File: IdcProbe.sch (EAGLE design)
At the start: 78 parts, among them P1 BANANA_SOCKETVERTICAL, P2 BANANA_SOCKETVERTICAL, Q1 PMV45EN, U1 TPS65131RGET, U2 NCP361MUTBG, U4 TL074D, X3 R141426

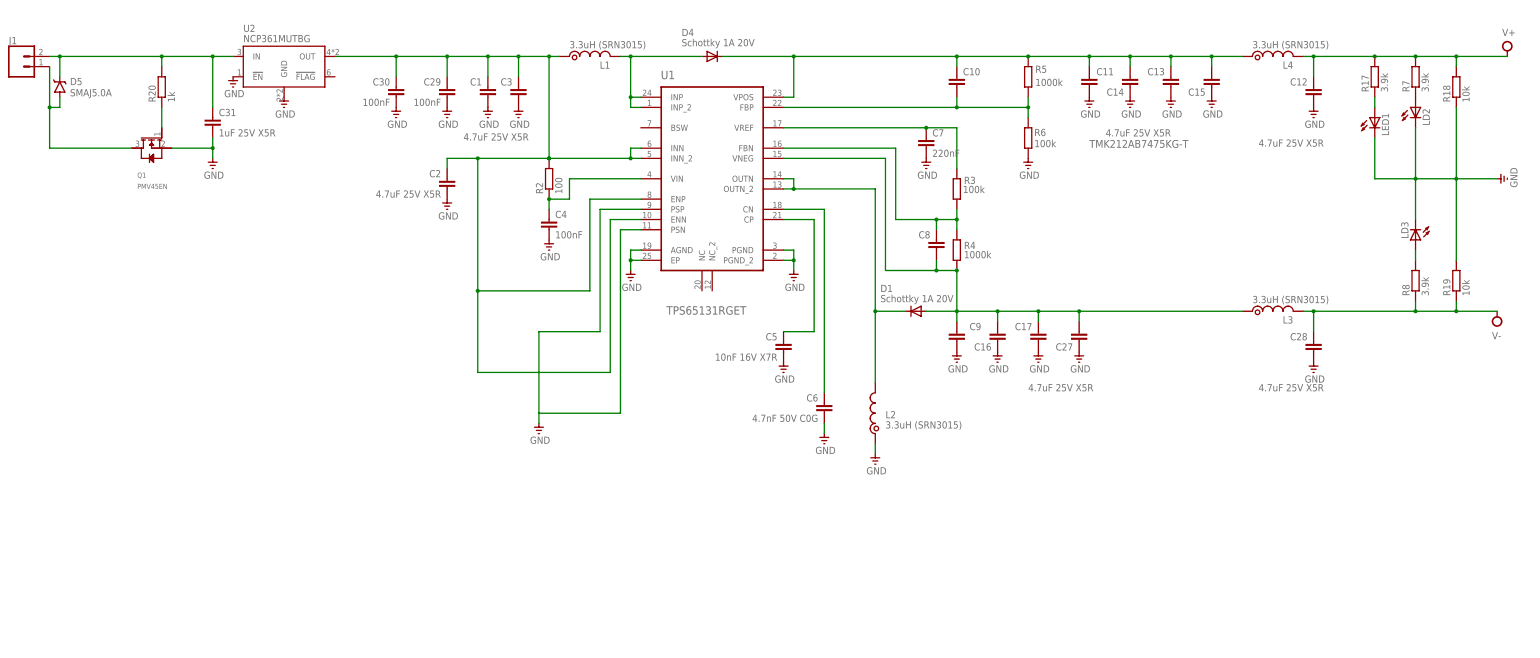
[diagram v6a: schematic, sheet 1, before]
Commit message: Update
Added fuse.
Renumbered schematic.
Created pdf and gerber for review.
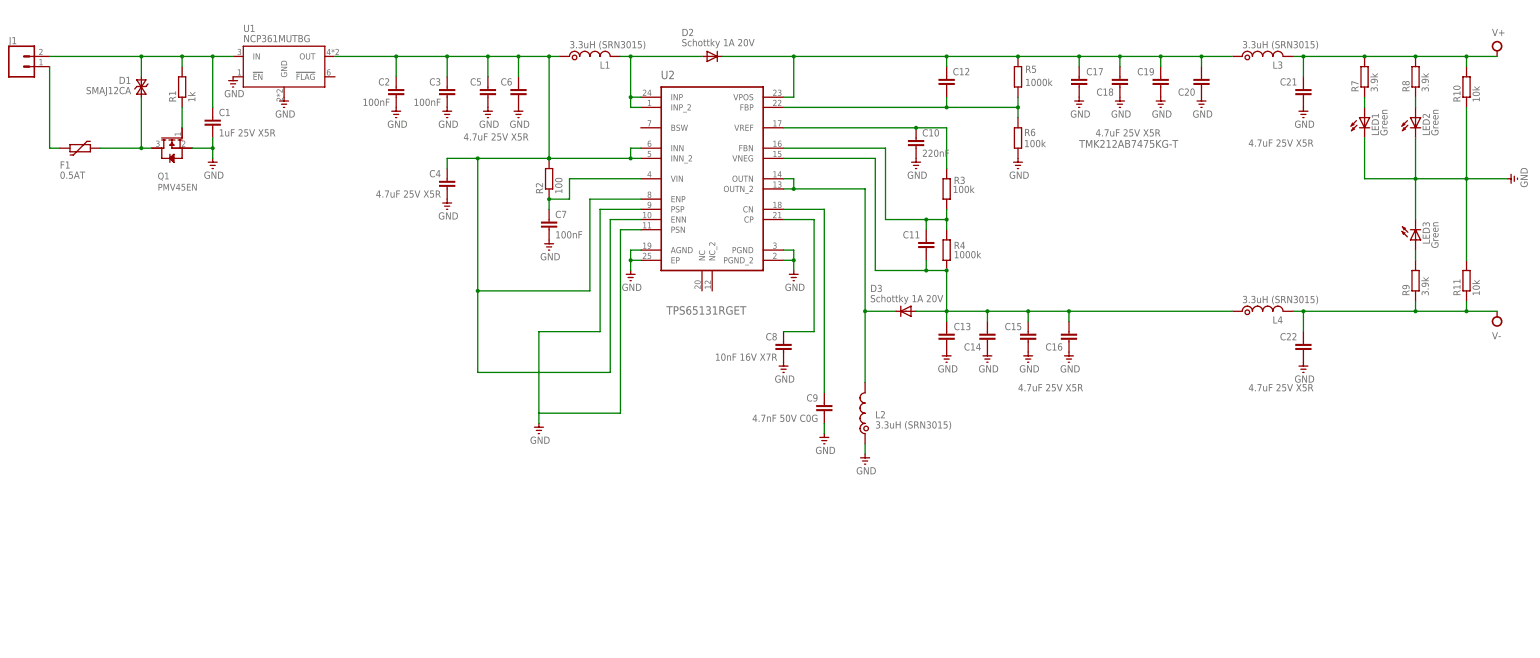
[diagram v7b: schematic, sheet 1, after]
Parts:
- removed D5: SMAJ5.0A, Jeroen:SMAJ13A-TR
- removed LD2: (no value), led:LEDCHIP-LED0805
- added D3: Schottky 1A 20V, diode:DIODE-SOD323-R
- added F1: 0.5AT, dp_devices:FUSE_PTC-0805
- added LED2: Green, led:LEDCHIP-LED0805
- C1: value 4.7uF 25V X5R -> 1uF 25V X5R
- C10: value (none) -> 220nF
- C11, C12, C28: value 4.7uF 25V X5R -> (none); MPN TMK212AB7475KG-T -> (none)
- C18, C19, C20, C4: value 100nF -> 4.7uF 25V X5R; MPN (none) -> TMK212AB7475KG-T
- C2, C27, C3: value 4.7uF 25V X5R -> 100nF; MPN TMK212AB7475KG-T -> (none)
- C21, C22: value 47uF (EEEFK1V470P) -> 4.7uF 25V X5R; device rcl:CPOL-EUD -> rcl:C-EUC0805; MPN (none) -> TMK212AB7475KG-T
- C23: value 3.3nF / 2.2nF -> 47uF (EEEFK1V470P); device rcl:C-EUC0805 -> rcl:CPOL-EUD
- C24: value (none) -> 47uF (EEEFK1V470P); device rcl:C-EUC0805 -> rcl:CPOL-EUD
- C25: value (none) -> 100nF
- C26: value (none) -> 3.3nF / 2.2nF
- C29: value 100nF -> (none)
- C31: value 1uF 25V X5R -> (none); MPN TMK212AB7475KG-T -> (none)
- C5: value 10nF 16V X7R -> 4.7uF 25V X5R; MPN (none) -> TMK212AB7475KG-T
- C6: value 4.7nF 50V C0G -> 4.7uF 25V X5R; MPN (none) -> TMK212AB7475KG-T
- C7: value 220nF -> 100nF
- C8: value (none) -> 10nF 16V X7R
- C9: value 4.7uF 25V X5R -> 4.7nF 50V C0G; MPN TMK212AB7475KG-T -> (none)
- D1: value Schottky 1A 20V -> SMAJ12CA; device diode:DIODE-SOD323-R -> Jeroen:TVS_BISMA; MPN PMEG4010BEA -> (none)
- LED1, LED3: value (none) -> Green
- R1: value 1K -> 1k; device rcl:R-EU_R0805 -> rcl:R-EU_R0805I
- R10: value (none) -> 10k; device rcl:R-EU_R0805 -> rcl:R-EU_R0805I
- R11: value 0 -> 10k; device rcl:R-EU_R0805 -> rcl:R-EU_R0805I
- R12: value 100k -> 15 / 33
- R13: value 10k -> (none); device rcl:R-EU_R0805I -> rcl:R-EU_R0805
- R14: value (none) -> 100k; device rcl:R-EU_R0805I -> Jeroen:POT_MULTI; MPN (none) -> 3386P-1-104LF
- R16: value 100k -> 1K; device Jeroen:POT_MULTI -> rcl:R-EU_R0805; MPN 3386P-1-104LF -> (none)
- R17: value 3.9k -> 10k
- R18, R19: value 10k -> (none)
- R20: value 1k -> 10k
- R21: value 10k -> 100k; device rcl:R-EU_R0805I -> rcl:R-EU_R0805
- R22: value (none) -> 0; device rcl:R-EU_R0805I -> rcl:R-EU_R0805
- R9: value 15 / 33 -> 3.9k; device rcl:R-EU_R0805 -> rcl:R-EU_R0805I
- U1: value TPS65131RGET -> NCP361MUTBG; device Jeroen:TPS65131RGET -> Jeroen:NCP36XMU; MPN (none) -> TMK212AB7475KG-T
- U2: value NCP361MUTBG -> TPS65131RGET; device Jeroen:NCP36XMU -> Jeroen:TPS65131RGET; MPN TMK212AB7475KG-T -> (none)
- renumbered D4 to D2, LD3 to LED3, U$1 to H1, U4 to IC1, X3 to X1
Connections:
- new net N$21: F1.2, J1.1
- net CN: now also C9.1, U2.CN; no longer C6.1, U1.CN
- net CP: now also C8.1, U2.CP; no longer C5.1, U1.CP
- net FBN: now also C11.1, U2.FBN; no longer C8.1, U1.FBN
- net FBP: now also C12.2, U2.FBP; no longer C10.2, U1.FBP
- net GND: now also C10.2, C18.2, C19.2, C20.2, C21.2, C22.2, C23.-, C24.+, C27.1, C28.1, C29.1, C31.1, C8.2, LED2.C, R10.1, R11.2, R19.1, R21.1, U1.!EN, U1.GND, U2.AGND, U2.EP, U2.PGND, U2.PGND_2, U2.PSN, U2.PSP; no longer C11.2, C12.2, C19.1, C20.1, C21.-, C22.+, C23.1, C24.1, C27.2, C28.2, C29.2, C30.2, C31.2, LD2.C, R12.1, R14.1, R19.2, R22.1, U1.AGND, U1.EP, U1.PGND, U1.PGND_2, U1.PSN, U1.PSP, U2.!EN, U2.GND
- net INP: now also U2.INP, U2.INP_2; no longer U1.INP, U1.INP_2
- net N$1: now also LED2.A, R8.1; no longer LD2.A, R7.1
- net N$10: now also C28.2, R13.2; no longer C25.2, R10.2
- net N$11: now also R20.2, R21.2, R22.1; no longer R11.1, R12.2, R13.2
- net N$12: now also C31.2, R22.2; no longer C26.2, R11.2
- net N$13: now also C29.2, R12.1, R13.1; no longer C24.2, R10.1, R9.1
- net N$14: now also R19.2, R20.1; no longer R13.1, R14.2
- net N$15: now also R14.SW; no longer R16.SW
- net N$16: now also R7.1; no longer R17.1
- net N$17: now also C1.1, D1.C, R1.2, U1.IN; no longer C31.1, D5.C, R20.2, U2.IN
- net N$18: now also D1.A, F1.1; no longer D5.A, J1.1
- net N$19: now also R1.1; no longer R20.1
- net N$2: now also R9.2; no longer R8.2
- net N$20: now also R17.2, R18.2; no longer R21.2, R22.2
- net N$3: now also R16.2, R17.1; no longer R1.2, R21.1
- net N$4: now also R16.1; no longer R1.1
- net N$9: now also C26.2, R12.2; no longer C23.2, R9.2
- net OUTN: now also D3.C, U2.OUTN, U2.OUTN_2; no longer D1.C, U1.OUTN, U1.OUTN_2
- net RV+: now also C12.1, C17.1, C18.1, C19.1, C20.1, L3.1, U2.VPOS; no longer C10.1, C11.1, C13.1, C14.1, C15.1, L4.1, U1.VPOS
- net RV-: now also C11.2, C13.1, C14.1, C15.1, D3.A, L4.1, U2.VNEG; no longer C17.1, C27.1, C8.2, C9.1, D1.A, L3.1, U1.VNEG
- net V+: now also C21.1, C23.+, C25.2, C30.2, L3.2, R10.2, R14.CW, R8.2; no longer C12.1, C18.2, C19.2, C21.+, L4.2, R16.CW, R17.2, R18.2
- net V-: now also C22.1, C24.-, C27.2, C30.1, L4.2, R11.1, R14.CCW, R9.1; no longer C18.1, C20.2, C22.-, C28.1, L3.2, R16.CCW, R19.1, R8.1
- net VI: now also C4.1, C5.1, C6.1, U1.OUT, U2.ENN, U2.ENP, U2.INN, U2.INN_2; no longer C1.1, C29.1, C30.1, U1.ENN, U1.ENP, U1.INN, U1.INN_2, U2.OUT
- net VIN: now also C7.1, U2.VIN; no longer C4.1, U1.VIN
- net VREF: now also C10.1, U2.VREF; no longer C7.1, U1.VREF
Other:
- note added: "(fuse to save USB on oscilloscope)"
- note added: "Clamp 20V"
- note added: "Last resort"
- note removed: "Clamp 7V"
- moved on the sheet: C1, C10, C11, C12, C13, C14, C15, C16, C17, C2, C25, C26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
